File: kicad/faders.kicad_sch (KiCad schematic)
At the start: 140 parts, among them J301 Conn_02x03_Counter_Clockwise, J302 Conn_01x06_Socket, J303 Conn_01x06_Socket, J307 Conn_01x06_Socket, J308 Conn_01x06_Socket, J309 Conn_01x05_Socket, J310 Conn_01x05_Socket, J311 Conn_01x06_Socket, J312 Conn_01x06_Socket, SW300 SW_SPST, SW301 SW_SPST, SW302 SW_SPST, SW303 SW_SPST, SW304 SW_SPST, SW400 RotaryEncoder_Switch, SW401 RotaryEncoder_Switch, SW402 RotaryEncoder_Switch, SW403 RotaryEncoder_Switch, SW404 RotaryEncoder_Switch, SW405 RotaryEncoder_Switch, SW406 RotaryEncoder_Switch, SW407 RotaryEncoder_Switch, SW408 RotaryEncoder_Switch, SW409 RotaryEncoder_Switch, SW410 SW_SPST, SW411 SW_SPST, SW412 SW_SPST, SW413 SW_SPST, SW414 SW_SPST, SW415 SW_SPST, SW416 SW_SPST, SW417 SW_SPST, SW418 SW_SPST, SW419 SW_SPST, U301 RP2040, U302 AT25SF081-SSHD-X, U303 MTCH105, U304 MCP3008, U305 LM4040D33, U306 PCA9635, U307 MCP23S17_SO, U308 DRV8871DDA, U309 DRV8871DDA, U310 DRV8871DDA, U311 DRV8871DDA, U312 DRV8871DDA, U401 MCP23S17_SO, U402 MCP23S17_SO, U403 MCP23S17_SO, U404 LS30, U405 LS30, U406 LS30, U407 LS30, U408 LS30, U409 LS30, U410 LS30, U411 LS30, U412 LS30, U413 LS30, X301 12Mhz

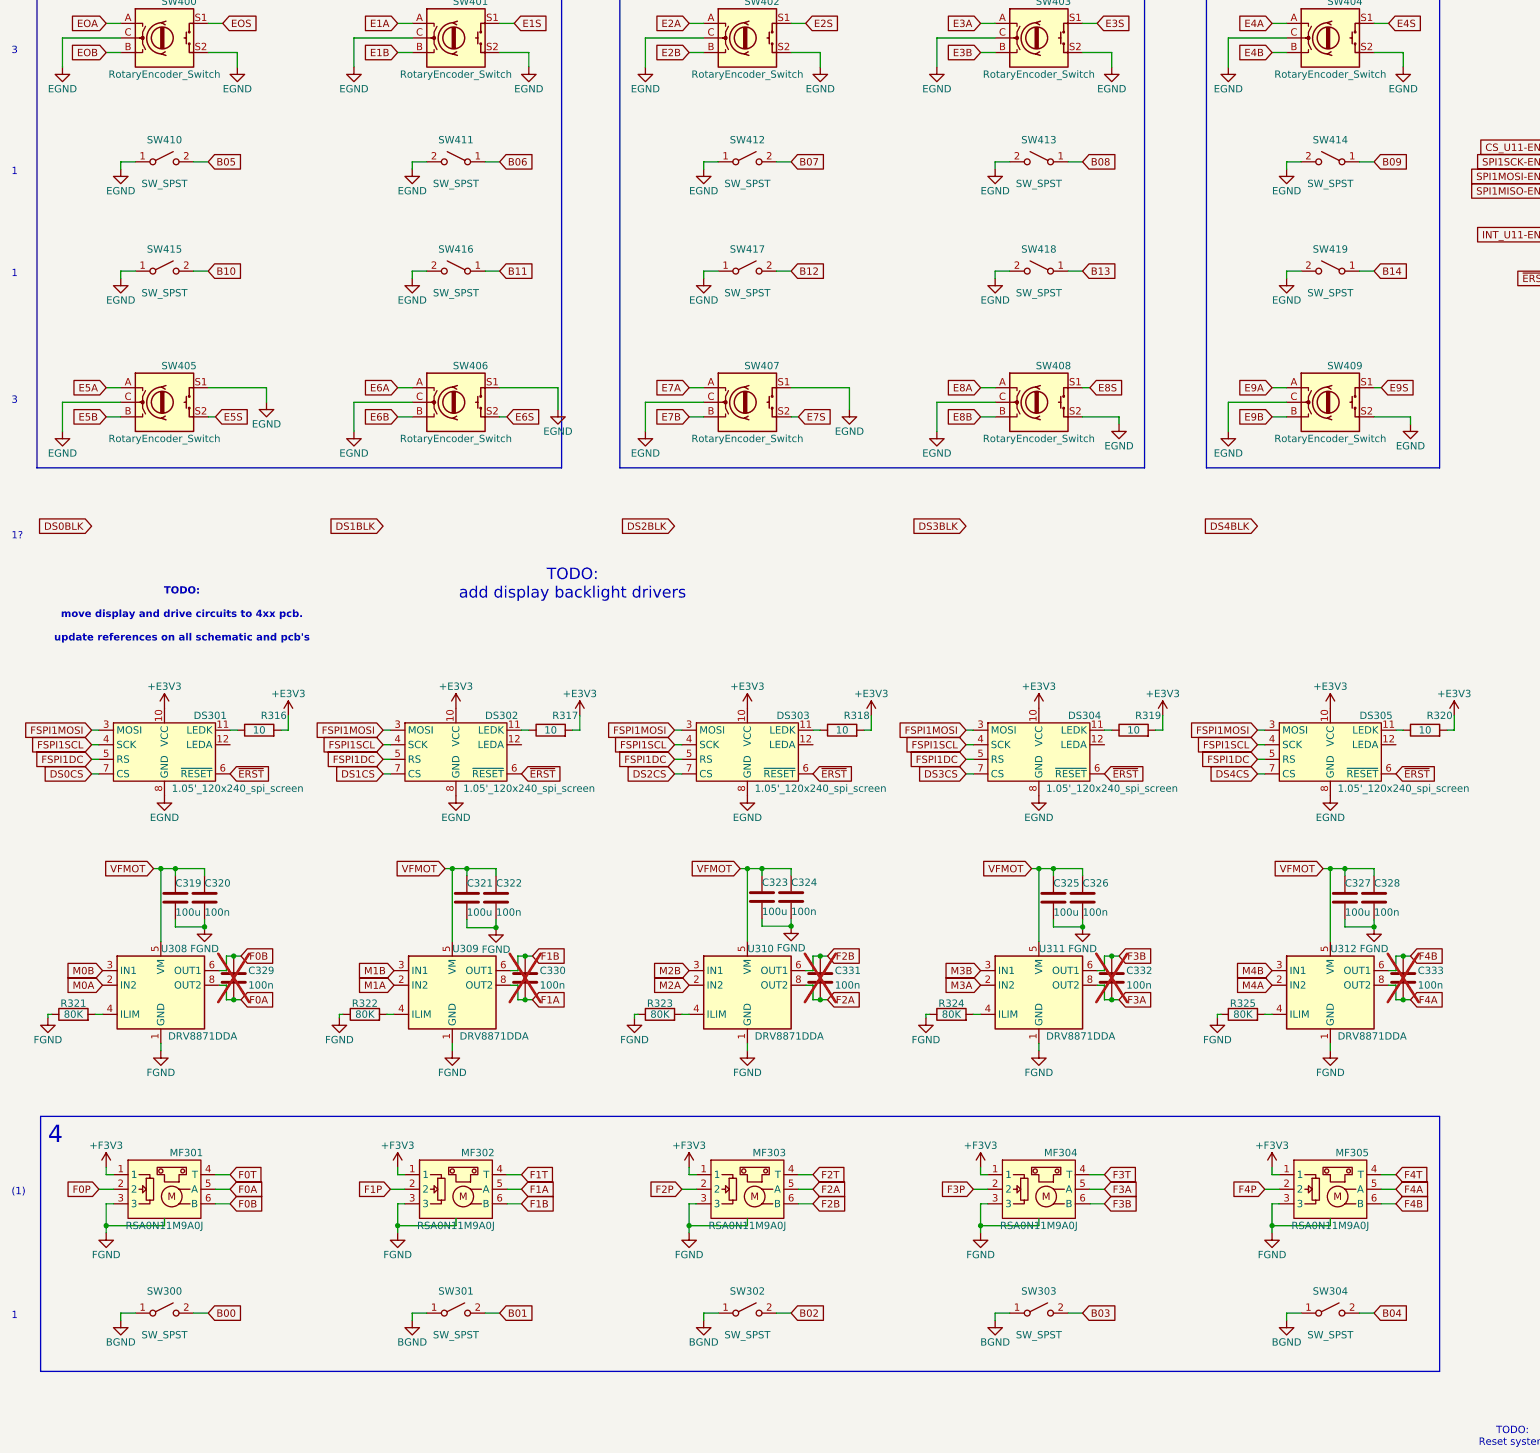
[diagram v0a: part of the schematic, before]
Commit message: replaced normal mx footprints to ones that also support hot swap sockets and have leds build in.
updated schematic and pcb to accomodate this. didn't connect the leds in the footprint yet
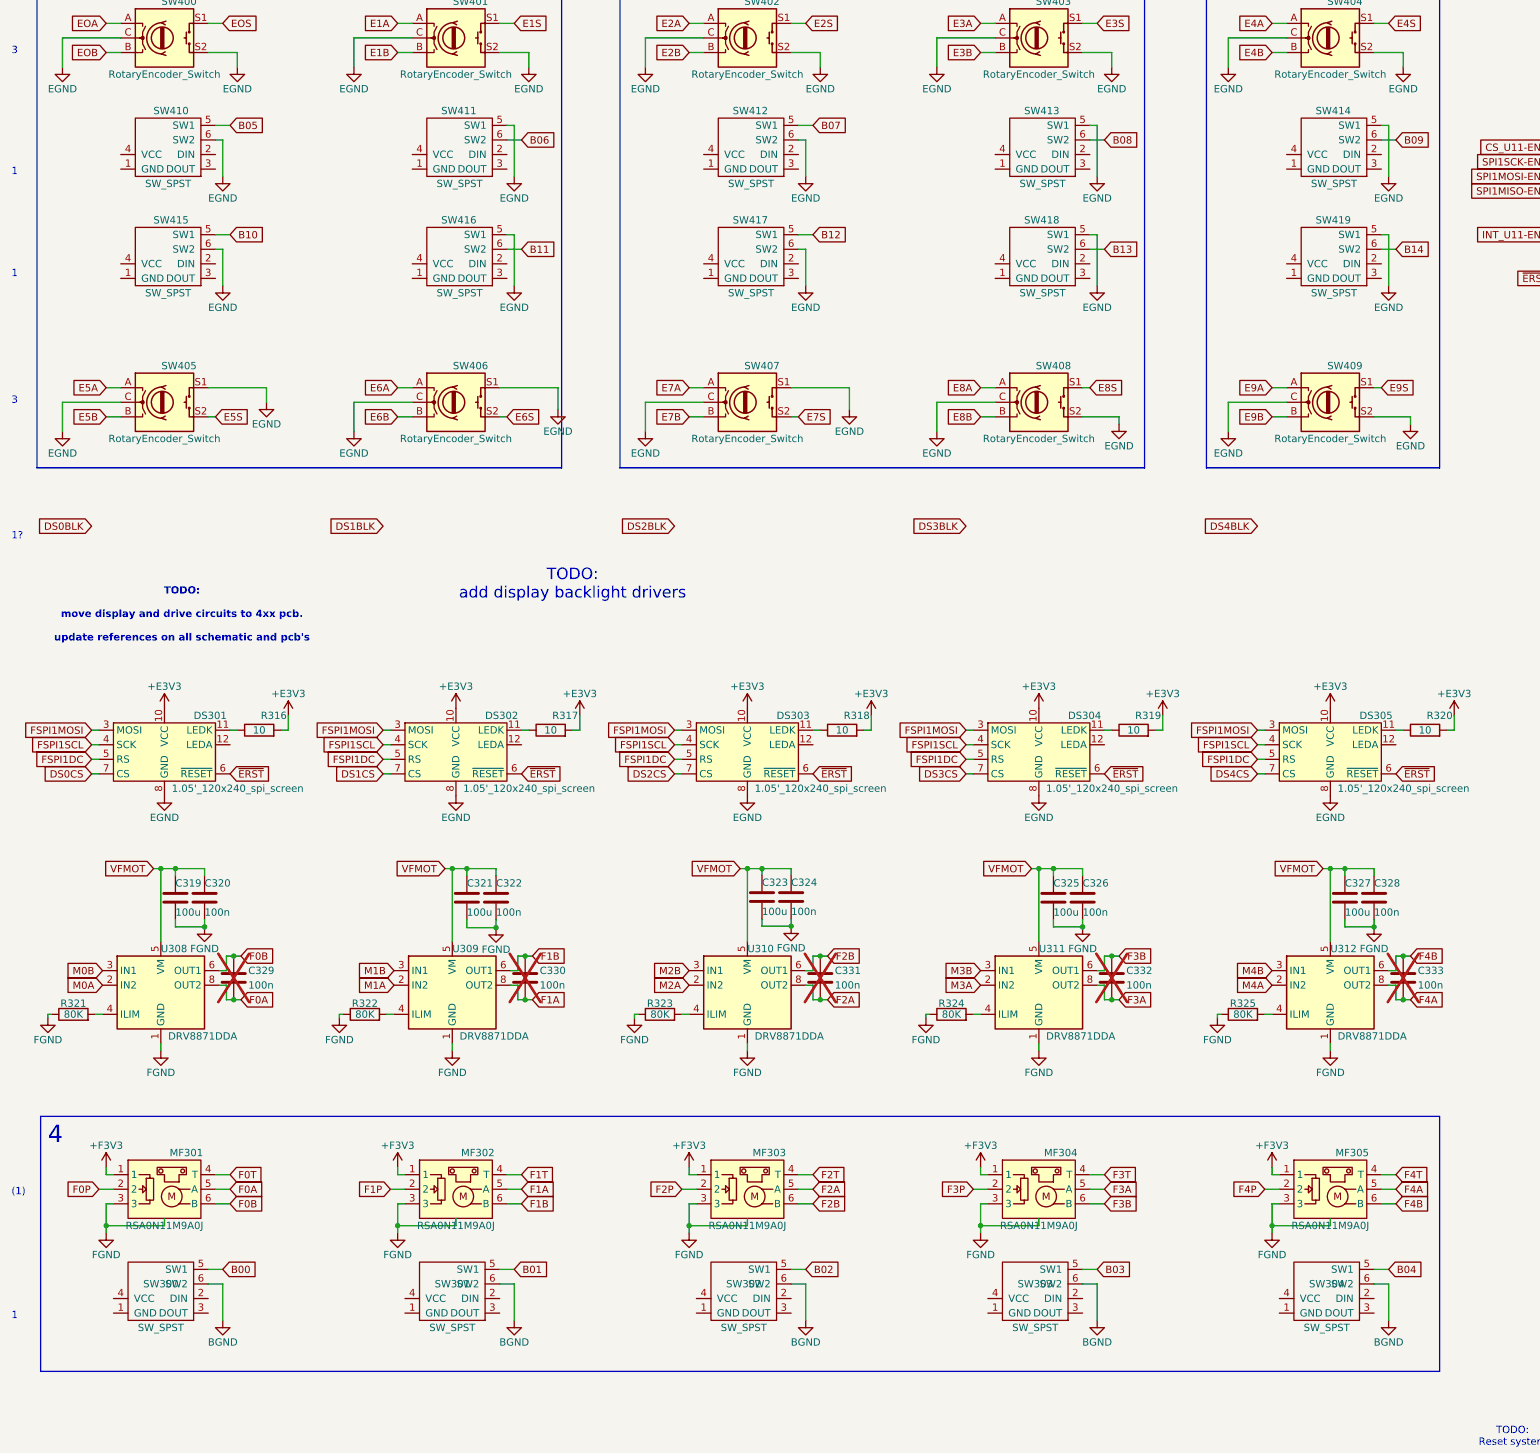
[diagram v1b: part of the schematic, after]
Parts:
- SW300, SW301, SW302, SW303, SW304, SW410, SW411, SW412, SW413, SW414, SW415, SW416, SW417, SW418, SW419: footprint Button_Switch_Keyboard:SW_Cherry_MX_1.00u_Plate -> Cherry MX:Cherry-MX_Plate-Mounted_LTST-A683CEGBW_Kailh_Socket; symbol Switch:SW_SPST -> Cherry_MX:Cherry_MX_RGB
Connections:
- net B00: now also SW300.5 (SW1); no longer SW300.2 (B)
- net B01: now also SW301.5 (SW1); no longer SW301.2 (B)
- net B02: now also SW302.5 (SW1); no longer SW302.2 (B)
- net B03: now also SW303.5 (SW1); no longer SW303.2 (B)
- net B04: now also SW304.5 (SW1); no longer SW304.2 (B)
- net B05: now also SW410.5 (SW1); no longer SW410.2 (B)
- net B06: now also SW411.6 (SW2); no longer SW411.1 (A)
- net B07: now also SW412.5 (SW1); no longer SW412.2 (B)
- net B08: now also SW413.6 (SW2); no longer SW413.1 (A)
- net B09: now also SW414.6 (SW2); no longer SW414.1 (A)
- net B10: now also SW415.5 (SW1); no longer SW415.2 (B)
- net B11: now also SW416.6 (SW2); no longer SW416.1 (A)
- net B12: now also SW417.5 (SW1); no longer SW417.2 (B)
- net B13: now also SW418.6 (SW2); no longer SW418.1 (A)
- net B14: now also SW419.6 (SW2); no longer SW419.1 (A)
- net BGND: now also SW300.6 (SW2), SW301.6 (SW2), SW302.6 (SW2), SW303.6 (SW2), SW304.6 (SW2); no longer SW300.1 (A), SW301.1 (A), SW302.1 (A), SW303.1 (A), SW304.1 (A)
- net EGND: now also SW410.6 (SW2), SW411.5 (SW1), SW412.6 (SW2), SW413.5 (SW1), SW414.5 (SW1), SW415.6 (SW2), SW416.5 (SW1), SW417.6 (SW2), SW418.5 (SW1), SW419.5 (SW1); no longer SW410.1 (A), SW411.2 (B), SW412.1 (A), SW413.2 (B), SW414.2 (B), SW415.1 (A), SW416.2 (B), SW417.1 (A), SW418.2 (B), SW419.2 (B)

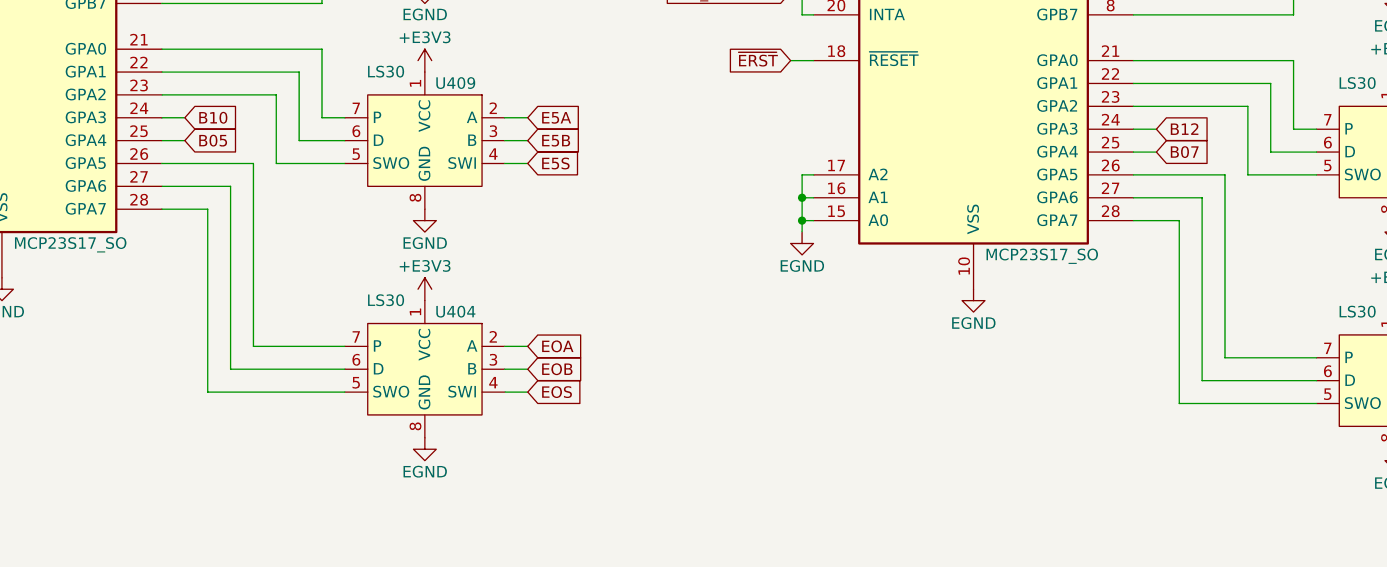
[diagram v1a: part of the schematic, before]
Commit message: more progress on fader pcb. moved around ls30's to make space for hot swap sockets
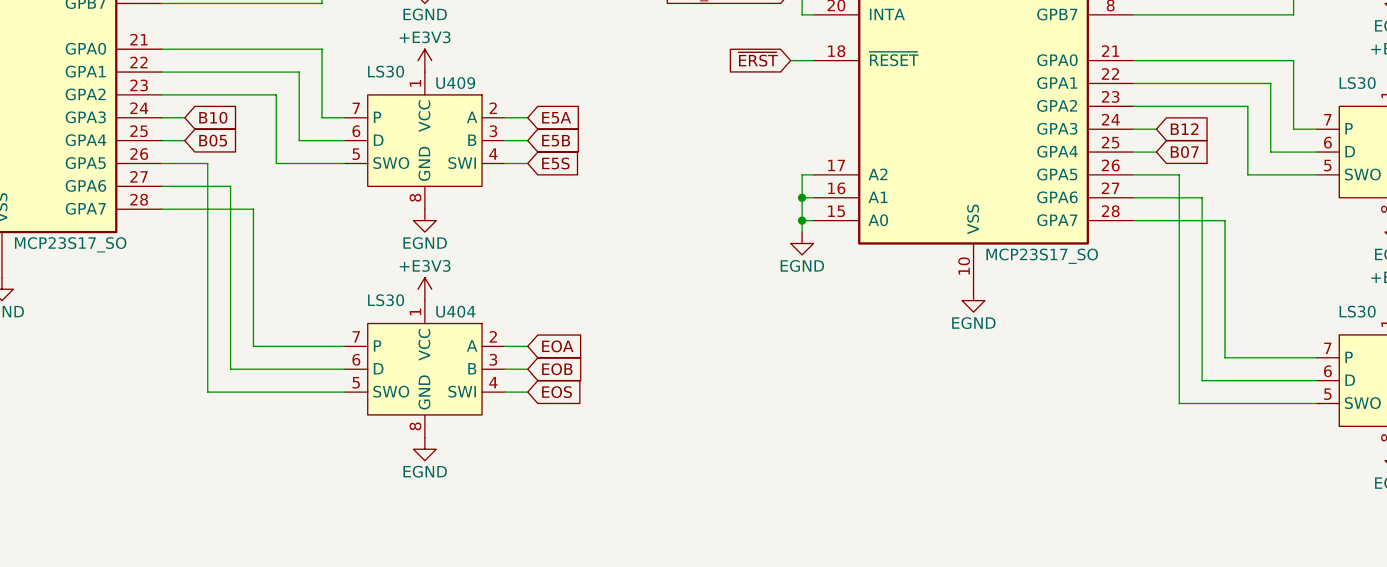
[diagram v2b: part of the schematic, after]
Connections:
- net at U402.26 (GPA5): now also U406.5 (SWO); no longer U406.7 (P)
- net at U402.28 (GPA7): now also U406.7 (P); no longer U406.5 (SWO)
- net at U401.26 (GPA5): now also U404.5 (SWO); no longer U404.7 (P)
- net at U401.28 (GPA7): now also U404.7 (P); no longer U404.5 (SWO)
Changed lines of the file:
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@@
 	(wire
 		(pts
-			(xy 320.04 83.82) (xy 327.66 83.82)
-		)
-		(stroke
-			(width 0)
-			(type default)
-		)
-	)
-	(wire
-		(pts
 			(xy 80.01 24.13) (xy 82.55 24.13)
 		)
@@
 	(wire
 		(pts
-			(xy 427.99 85.09) (xy 435.61 85.09)
-		)
-		(stroke
-			(width 0)
-			(type default)
-		)
-	)
-	(wire
-		(pts
 			(xy 228.6 374.65) (xy 227.33 374.65)
 		)
@@
 	(wire
 		(pts
+			(xy 330.2 86.36) (xy 330.2 101.6)
+		)
+		(stroke
+			(width 0)
+			(type default)
+		)
+	)
+	(wire
+		(pts
 			(xy 353.06 177.8) (xy 353.06 179.07)
 		)
@@
 	(wire
 		(pts
+			(xy 433.07 82.55) (xy 427.99 82.55)
+		)
+		(stroke
+			(width 0)
+			(type default)
+		)
+	)
+	(wire
+		(pts
 			(xy 327.66 234.95) (xy 356.87 234.95)
 		)
@@
 	(wire
 		(pts
-			(xy 438.15 82.55) (xy 438.15 102.87)
-		)
-		(stroke
-			(width 0)
-			(type default)
-		)
-	)
-	(wire
-		(pts
 			(xy 27.94 149.86) (xy 26.67 149.86)
 		)
@@
 	(wire
 		(pts
-			(xy 427.99 82.55) (xy 438.15 82.55)
-		)
-		(stroke
-			(width 0)
-			(type default)
-		)
-	)
-	(wire
-		(pts
 			(xy 335.28 78.74) (xy 340.36 78.74)
 		)
@@
 	(wire
 		(pts
+			(xy 427.99 87.63) (xy 438.15 87.63)
+		)
+		(stroke
+			(width 0)
+			(type default)
+		)
+	)
+	(wire
+		(pts
 			(xy 335.28 60.96) (xy 335.28 53.34)
 		)
@@
 	(wire
 		(pts
+			(xy 330.2 86.36) (xy 320.04 86.36)
+		)
+		(stroke
+			(width 0)
+			(type default)
+		)
+	)
+	(wire
+		(pts
 			(xy 180.34 152.4) (xy 179.07 152.4)
 		)
@@
 	(wire
 		(pts
-			(xy 320.04 81.28) (xy 330.2 81.28)
-		)
-		(stroke
-			(width 0)
-			(type default)
-		)
-	)
-	(wire
-		(pts
 			(xy 435.61 49.53) (xy 435.61 29.21)
 		)
@@
 	(wire
 		(pts
+			(xy 438.15 87.63) (xy 438.15 102.87)
+		)
+		(stroke
+			(width 0)
+			(type default)
+		)
+	)
+	(wire
+		(pts
 			(xy 407.67 240.03) (xy 410.21 240.03)
 		)
@@
 	(wire
 		(pts
-			(xy 325.12 106.68) (xy 325.12 86.36)
+			(xy 325.12 81.28) (xy 325.12 106.68)
 		)
 		(stroke
@@
 	(wire
 		(pts
+			(xy 427.99 85.09) (xy 435.61 85.09)
+		)
+		(stroke
+			(width 0)
+			(type default)
+		)
+	)
+	(wire
+		(pts
 			(xy 420.37 171.45) (xy 420.37 172.72)
 		)
@@
 	(wire
 		(pts
-			(xy 148.59 241.3) (xy 151.13 241.3)
+			(xy 325.12 81.28) (xy 320.04 81.28)
 		)
 		(stroke
@@
 	(wire
 		(pts
-			(xy 271.78 354.33) (xy 269.24 354.33)
+			(xy 148.59 241.3) (xy 151.13 241.3)
 		)
 		(stroke
@@
 	(wire
 		(pts
-			(xy 146.05 350.52) (xy 140.97 350.52)
+			(xy 271.78 354.33) (xy 269.24 354.33)
 		)
 		(stroke
@@
 	(wire
 		(pts
-			(xy 199.39 92.71) (xy 205.74 92.71)
+			(xy 146.05 350.52) (xy 140.97 350.52)
 		)
 		(stroke
@@
 	(wire
 		(pts
-			(xy 330.2 222.25) (xy 356.87 222.25)
+			(xy 199.39 92.71) (xy 205.74 92.71)
 		)
 		(stroke
@@
 	(wire
 		(pts
-			(xy 500.38 318.77) (xy 502.92 318.77)
+			(xy 330.2 222.25) (xy 356.87 222.25)
 		)
 		(stroke
@@
 	(wire
 		(pts
-			(xy 68.58 383.54) (xy 72.39 383.54)
+			(xy 500.38 318.77) (xy 502.92 318.77)
 		)
 		(stroke
@@
 	(wire
 		(pts
-			(xy 320.04 86.36) (xy 325.12 86.36)
+			(xy 68.58 383.54) (xy 72.39 383.54)
 		)
 		(stroke
@@
 		)
 	)
-	(polyline
+	(wire
 		(pts
-			(xy 243.84 369.57) (xy 248.92 369.57)
+			(xy 320.04 83.82) (xy 327.66 83.82)
 		)
 		(stroke
@@
 		)
 	)
-	(wire
+	(polyline
 		(pts
-			(xy 535.94 57.15) (xy 538.48 57.15)
+			(xy 243.84 369.57) (xy 248.92 369.57)
 		)
 		(stroke
@@
 	(wire
 		(pts
-			(xy 97.79 92.71) (xy 99.06 92.71)
+			(xy 535.94 57.15) (xy 538.48 57.15)
 		)
 		(stroke
@@
 	(wire
 		(pts
-			(xy 69.85 378.46) (xy 76.2 378.46)
+			(xy 97.79 92.71) (xy 99.06 92.71)
 		)
 		(stroke
@@
 	(wire
 		(pts
-			(xy 396.24 171.45) (xy 396.24 190.5)
+			(xy 69.85 378.46) (xy 76.2 378.46)
 		)
 		(stroke
@@
 	(wire
 		(pts
-			(xy 330.2 81.28) (xy 330.2 101.6)
+			(xy 396.24 171.45) (xy 396.24 190.5)
 		)
 		(stroke
@@
 	(wire
 		(pts
-			(xy 433.07 107.95) (xy 433.07 87.63)
+			(xy 433.07 82.55) (xy 433.07 107.95)
 		)
 		(stroke
@@
 	(wire
 		(pts
-			(xy 427.99 87.63) (xy 433.07 87.63)
-		)
-		(stroke
-			(width 0)
-			(type default)
-		)
-	)
-	(wire
-		(pts
 			(xy 427.99 62.23) (xy 443.23 62.23)
 		)
@@
 				)
 			)
+			(project "midi-controller"
+				(path "/2cba2024-755f-4534-8b6f-a95a551957b1/f0e0d697-e432-4b50-8287-c9353a450074"
+					(reference "#PWR?")
+					(unit 1)
+				)
+			)
 		)
 	)
@@
 				)
 			)
+			(project "midi-controller"
+				(path "/2cba2024-755f-4534-8b6f-a95a551957b1/f0e0d697-e432-4b50-8287-c9353a450074"
+					(reference "#PWR?")
+					(unit 1)
+				)
+			)
 		)
 	)
@@
 				)
 			)
+			(project "midi-controller"
+				(path "/2cba2024-755f-4534-8b6f-a95a551957b1/f0e0d697-e432-4b50-8287-c9353a450074"
+					(reference "#PWR?")
+					(unit 1)
+				)
+			)
 		)
 	)
@@
 				)
 			)
+			(project "midi-controller"
+				(path "/2cba2024-755f-4534-8b6f-a95a551957b1/f0e0d697-e432-4b50-8287-c9353a450074"
+					(reference "#PWR?")
+					(unit 1)
+				)
+			)
 		)
 	)
@@
 				)
 			)
+			(project "midi-controller"
+				(path "/2cba2024-755f-4534-8b6f-a95a551957b1/f0e0d697-e432-4b50-8287-c9353a450074"
+					(reference "#PWR?")
+					(unit 1)
+				)
+			)
 		)
 	)
@@
 				)
 			)
+			(project "midi-controller"
+				(path "/2cba2024-755f-4534-8b6f-a95a551957b1/f0e0d697-e432-4b50-8287-c9353a450074"
+					(reference "#PWR?")
+					(unit 1)
+				)
+			)
 		)
 	)
@@
 				)
 			)
+			(project "midi-controller"
+				(path "/2cba2024-755f-4534-8b6f-a95a551957b1/f0e0d697-e432-4b50-8287-c9353a450074"
+					(reference "#PWR?")
+					(unit 1)
+				)
+			)
 		)
 	)
@@
 				)
 			)
+			(project "midi-controller"
+				(path "/2cba2024-755f-4534-8b6f-a95a551957b1/f0e0d697-e432-4b50-8287-c9353a450074"
+					(reference "#PWR?")
+					(unit 1)
+				)
+			)
 		)
 	)
@@
 				)
 			)
+			(project "midi-controller"
+				(path "/2cba2024-755f-4534-8b6f-a95a551957b1/f0e0d697-e432-4b50-8287-c9353a450074"
+					(reference "#PWR?")
+					(unit 1)
+				)
+			)
 		)
 	)
@@
 				)
 			)
+			(project "midi-controller"
+				(path "/2cba2024-755f-4534-8b6f-a95a551957b1/f0e0d697-e432-4b50-8287-c9353a450074"
+					(reference "#PWR?")
+					(unit 1)
+				)
+			)
 		)
 	)
@@
 				)
 			)
+			(project "midi-controller"
+				(path "/2cba2024-755f-4534-8b6f-a95a551957b1/f0e0d697-e432-4b50-8287-c9353a450074"
+					(reference "#PWR?")
+					(unit 1)
+				)
+			)
 		)
 	)
@@
 				)
 			)
+			(project "midi-controller"
+				(path "/2cba2024-755f-4534-8b6f-a95a551957b1/f0e0d697-e432-4b50-8287-c9353a450074"
+					(reference "#PWR?")
+					(unit 1)
+				)
+			)
 		)
 	)
@@
 				)
 			)
+			(project "midi-controller"
+				(path "/2cba2024-755f-4534-8b6f-a95a551957b1/f0e0d697-e432-4b50-8287-c9353a450074"
+					(reference "#PWR?")
+					(unit 1)
+				)
+			)
 		)
 	)
@@
 					(unit 1)
 				)
+			)
+			(project "midi-controller"
+				(path "/2cba2024-755f-4534-8b6f-a95a551957b1/f0e0d697-e432-4b50-8287-c9353a450074"
+					(reference "#PWR?")
+					(unit 1)
+				)
